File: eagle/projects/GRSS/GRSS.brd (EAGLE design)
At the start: 66 x 62.1 mm, 37 parts, among them J1 MOL-SL-2-RA, J10 MOL-SL-2-RA, J11 MOL-SL-2-V, J2 MOL-SL-2-RA, J3 MOL-SL-2-RA, J4 MOL-SL-2-RA, J5 MOL-SL-2-RA, J6 MOL-SL-2-RA, J7 MOL-SL-2-RA, J8 MOL-SL-2-RA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

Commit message: Squad Logo / 2-layer
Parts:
- removed IMAGE1: SQUAD_LOGO, grss:SQUAD_LOGO
- added LOGO1: (no value), grss:SQUAD_LOGO
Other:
- board text added: "Lincoln Glauser P17105: HABIP SPRING 2017 XXX-XXX-XX"
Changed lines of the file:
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@@
 <text x="16.2" y="28.1" size="1.016" layer="25" ratio="15">LDO</text>
 <text x="34.1" y="28.5" size="1.016" layer="25" ratio="15">555</text>
+<text x="48.5" y="32.6" size="1.016" layer="21" ratio="15">Lincoln Glauser
+P17105: HABIP
+SPRING 2017
+XXX-XXX-XX</text>
 </plain>
 <attributes>
@@
 <attribute name="VALUE" x="49.56" y="23.5" size="0.254" layer="27" ratio="6" align="center"/>
 </element>
-<element name="IMAGE1" library="grss" package="SQUAD_LOGO" value="SQUAD_LOGO" x="41.6" y="33.3"/>
+<element name="LOGO1" library="grss" package="SQUAD_LOGO" value="" x="41.2" y="34.1">
+<attribute name="_EXTERNAL_" value="" x="41.2" y="34.1" size="1.778" layer="27" display="off"/>
+</element>
 </elements>
 <signals>
@@
 </board>
 </drawing>
+<compatibility>
+<note version="6.3" minversion="6.2.2" severity="warning">
+Since Version 6.2.2 text objects can contain more than one line,
+which will not be processed correctly with this version.
+</note>
+</compatibility>
 </eagle>

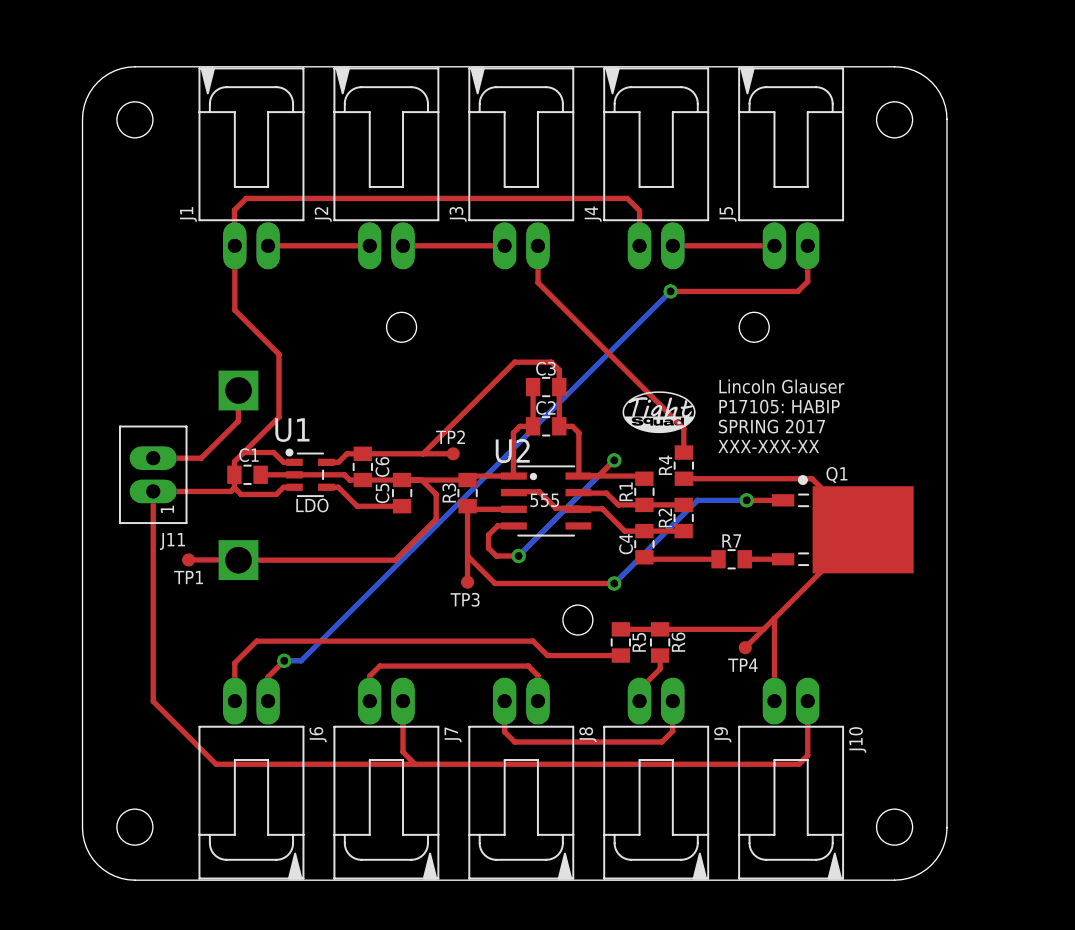
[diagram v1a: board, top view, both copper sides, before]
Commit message: GND / Power Planes - LG
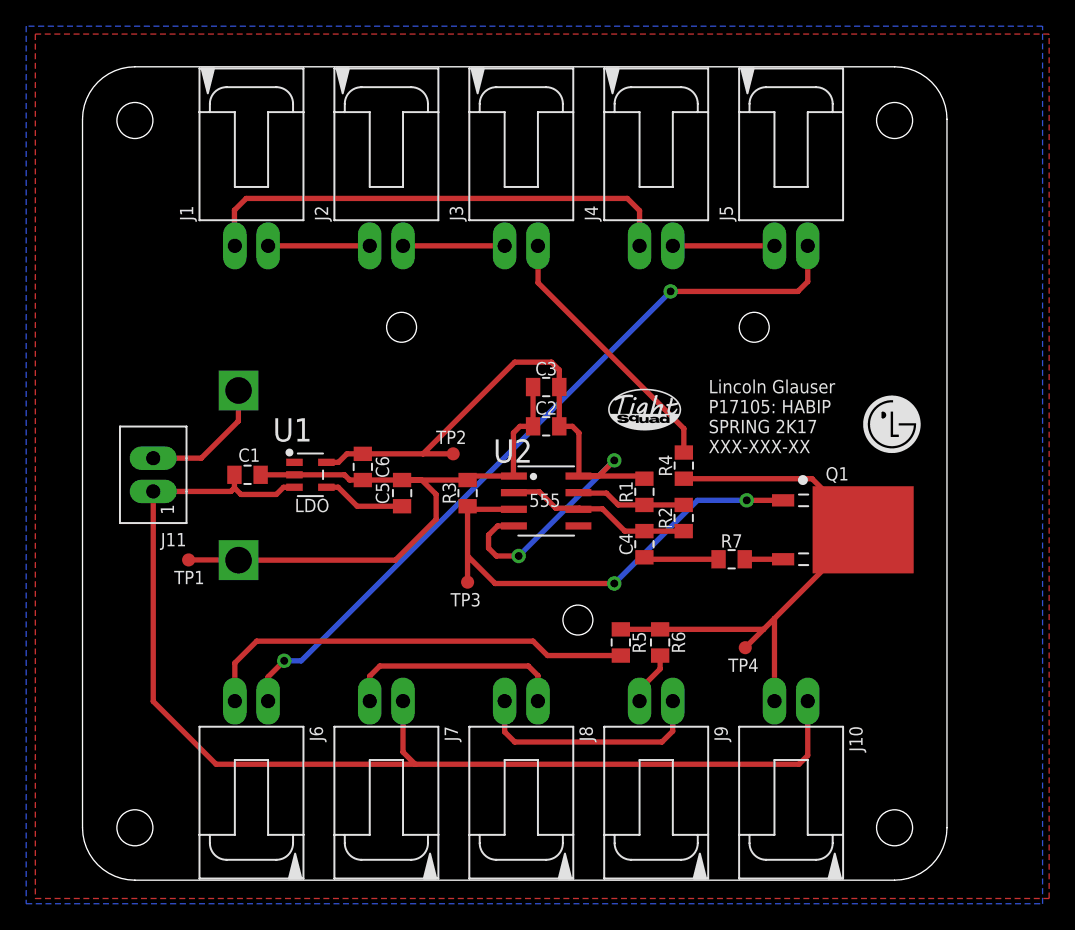
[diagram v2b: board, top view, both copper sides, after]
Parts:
- added E$1: (no value), grss:LG
- moved LOGO1 1.12 mm to (40.1, 34.3)
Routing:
- net 9V0: track 151.5 -> 127.1 mm
- added copper zone on layer 1, net 9V0
- added copper zone on layer 16, net GND
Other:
- board text added: "Lincoln Glauser P17105: HABIP SPRING 2K17 XXX-XXX-XX"
- board text removed: "Lincoln Glauser P17105: HABIP SPRING 2017 XXX-XXX-XX"
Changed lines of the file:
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@@
 <layers>
 <layer number="1" name="Top" color="4" fill="1" visible="yes" active="yes"/>
-<layer number="2" name="Route2" color="1" fill="3" visible="yes" active="yes"/>
+<layer number="2" name="Route2" color="1" fill="3" visible="no" active="no"/>
 <layer number="3" name="Route3" color="4" fill="3" visible="no" active="no"/>
 <layer number="14" name="Route14" color="1" fill="6" visible="no" active="no"/>
-<layer number="15" name="Route15" color="4" fill="6" visible="yes" active="yes"/>
+<layer number="15" name="Route15" color="4" fill="6" visible="no" active="no"/>
 <layer number="16" name="Bottom" color="1" fill="1" visible="yes" active="yes"/>
 <layer number="17" name="Pads" color="2" fill="1" visible="yes" active="yes"/>
@@
 <text x="16.2" y="28.1" size="1.016" layer="25" ratio="15">LDO</text>
 <text x="34.1" y="28.5" size="1.016" layer="25" ratio="15">555</text>
-<text x="48.5" y="32.6" size="1.016" layer="21" ratio="15">Lincoln Glauser
+<text x="47.8" y="32.6" size="1.016" layer="21" ratio="15">Lincoln Glauser
 P17105: HABIP
-SPRING 2017
+SPRING 2K17
 XXX-XXX-XX</text>
 </plain>
@@
 </class>
 </classes>
-<designrules name="4layer_4pcb">
+<designrules name="2layer_2pcb">
 <description language="de">&lt;b&gt;EAGLE Design Rules&lt;/b&gt;
 &lt;p&gt;
@@
 <description language="en">&lt;b&gt;EAGLE Design Rules&lt;/b&gt;
 &lt;p&gt;
-Modified for $66 4-layer student special from Advanced Circuits as of 02/07/2017. These specs also meet the standard specs at PCBWay as of 02/07/2017</description>
-<param name="layerSetup" value="(1+2*15+16)"/>
+Modified for $66 4-layer student special from Advanced Circuits as of 02/07/2017. These specs also meet the standard specs at PCBWay as of 02/07/2017. Updated layerSetup for 2-layer.</description>
+<param name="layerSetup" value="(1+16)"/>
 <param name="mtCopper" value="0.035mm 0.035mm 0.035559375mm 0.035559375mm 0.035559375mm 0.035559375mm 0.035559375mm 0.035559375mm 0.035559375mm 0.035559375mm 0.035559375mm 0.035559375mm 0.035559375mm 0.035559375mm 0.035mm 0.035mm"/>
 <param name="mtIsolate" value="0.486mm 0.488mm 0.200659375mm 0.149859375mm 0.200659375mm 0.149859375mm 0.200659375mm 0.149859375mm 0.200659375mm 0.149859375mm 0.200659375mm 0.149859375mm 0.200659375mm 0.149859375mm 0.486mm"/>
@@
 <attribute name="VALUE" x="51.119" y="16.942" size="0.254" layer="27" ratio="6"/>
 </element>
-<element name="H1" library="grss" package="2,75_HOLE_RASPI" value="MOUNT-HOLE_2.75" x="4" y="4.05"/>
-<element name="H2" library="grss" package="2,75_HOLE_RASPI" value="MOUNT-HOLE_2.75" x="62" y="4.05"/>
-<element name="H3" library="grss" package="2,75_HOLE_RASPI" value="MOUNT-HOLE_2.75" x="4" y="58.05"/>
-<element name="H4" library="grss" package="2,75_HOLE_RASPI" value="MOUNT-HOLE_2.75" x="62" y="58.05"/>
+<element name="H1" library="grss" package="2,75_HOLE_RASPI" value="MOUNT-HOLE_2.75" x="4" y="4"/>
+<element name="H2" library="grss" package="2,75_HOLE_RASPI" value="MOUNT-HOLE_2.75" x="62" y="4"/>
+<element name="H3" library="grss" package="2,75_HOLE_RASPI" value="MOUNT-HOLE_2.75" x="4" y="58"/>
+<element name="H4" library="grss" package="2,75_HOLE_RASPI" value="MOUNT-HOLE_2.75" x="62" y="58"/>
 <element name="R3" library="grss" package="R0805" value="4.7k" x="29.4" y="29.55" smashed="yes" rot="R270">
 <attribute name="TOLERANCE" value="1%" x="29.4" y="29.55" size="1.778" layer="27" rot="R270" display="off"/>
@@
 <attribute name="VALUE" x="49.56" y="23.5" size="0.254" layer="27" ratio="6" align="center"/>
 </element>
-<element name="LOGO1" library="grss" package="SQUAD_LOGO" value="" x="41.2" y="34.1">
-<attribute name="_EXTERNAL_" value="" x="41.2" y="34.1" size="1.778" layer="27" display="off"/>
-</element>
+<element name="LOGO1" library="grss" package="SQUAD_LOGO" value="" x="40.1" y="34.3">
+<attribute name="_EXTERNAL_" value="" x="40.1" y="34.3" size="1.778" layer="27" display="off"/>
+</element>
+<element name="E$1" library="grss" package="LG" value="" x="59.6" y="32.6"/>
 </elements>
 <signals>
@@
 <contactref element="J10" pad="1"/>
 <contactref element="J11" pad="1"/>
-<wire x1="16.1808" y1="31.9025" x2="16.1293" y2="31.901" width="0.4064" layer="1"/>
-<wire x1="16.1293" y1="31.901" x2="15.349" y2="31.901" width="0.4064" layer="1"/>
-<wire x1="15.349" y1="31.901" x2="14.6" y2="32.65" width="0.4064" layer="1"/>
-<wire x1="14.6" y1="32.65" x2="12.3" y2="32.65" width="0.4064" layer="1"/>
-<wire x1="12.3" y1="32.65" x2="11.6" y2="31.95" width="0.4064" layer="1"/>
-<wire x1="11.6" y1="31.95" x2="11.6" y2="30.95" width="0.4064" layer="1"/>
 <wire x1="11.6" y1="29.95" x2="11.6" y2="30.95" width="0.4064" layer="1"/>
 <wire x1="16.1808" y1="29.9975" x2="15.3475" y2="29.9975" width="0.4064" layer="1"/>
@@
 <wire x1="11.6" y1="51.15" x2="11.6" y2="48.46" width="0.4064" layer="1"/>
 <wire x1="11.6" y1="48.46" x2="11.63" y2="48.43" width="0.4064" layer="1"/>
-<wire x1="11.63" y1="48.43" x2="11.63" y2="43.52" width="0.4064" layer="1"/>
-<wire x1="11.63" y1="43.52" x2="15" y2="40.15" width="0.4064" layer="1"/>
-<wire x1="15" y1="40.15" x2="15" y2="35.35" width="0.4064" layer="1"/>
-<wire x1="15" y1="35.35" x2="12.3" y2="32.65" width="0.4064" layer="1"/>
 <wire x1="5.4" y1="29.68" x2="11.33" y2="29.68" width="0.4064" layer="1"/>
 <wire x1="11.33" y1="29.68" x2="11.6" y2="29.95" width="0.4064" layer="1"/>
@@
 <wire x1="5.4" y1="13.65" x2="5.4" y2="29.68" width="0.4064" layer="1"/>
 <wire x1="24.47" y1="9.78" x2="25.4" y2="8.85" width="0.4064" layer="1"/>
+<polygon width="0.4064" layer="1">
+<vertex x="-3.6" y="64.6"/>
+<vertex x="-3.6" y="-1.4"/>
+<vertex x="73.8" y="-1.4"/>
+<vertex x="73.8" y="64.6"/>
+</polygon>
 </signal>
 <signal name="GND">
@@
 <wire x1="25.9" y1="30.55" x2="24.4" y2="30.55" width="0.4064" layer="1"/>
 <wire x1="29.4" y1="30.55" x2="24.4" y2="30.55" width="0.4064" layer="1"/>
-<wire x1="32.9362" y1="30.855" x2="42.9" y2="24.65" width="0" layer="19" extent="1-1"/>
 <wire x1="8.1" y1="24.45" x2="11.896" y2="24.45" width="0.4064" layer="1"/>
 <wire x1="11.896" y1="24.45" x2="11.914" y2="24.432" width="0.4064" layer="1"/>
+<polygon width="0.4064" layer="16">
+<vertex x="-4.3" y="65.2"/>
+<vertex x="-4.3" y="-1.8"/>
+<vertex x="73.3" y="-1.8"/>
+<vertex x="73.3" y="65.2"/>
+</polygon>
+<wire x1="32.9362" y1="30.855" x2="42.9" y2="24.65" width="0" layer="19" extent="1-1"/>
 </signal>
 <signal name="THRTRIG">

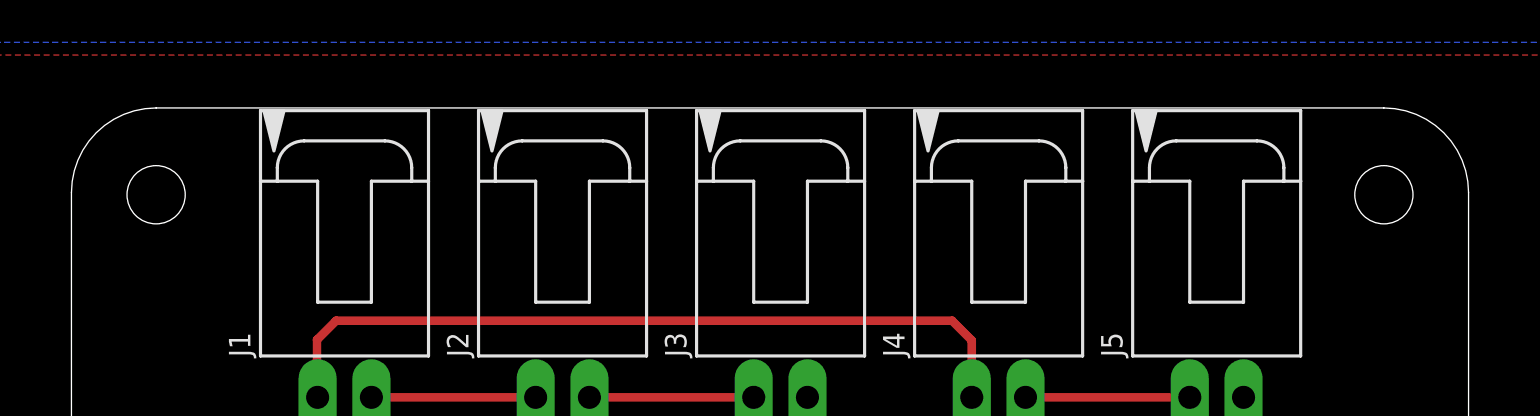
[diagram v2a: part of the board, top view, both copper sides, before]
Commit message: moved mounting holes briefly
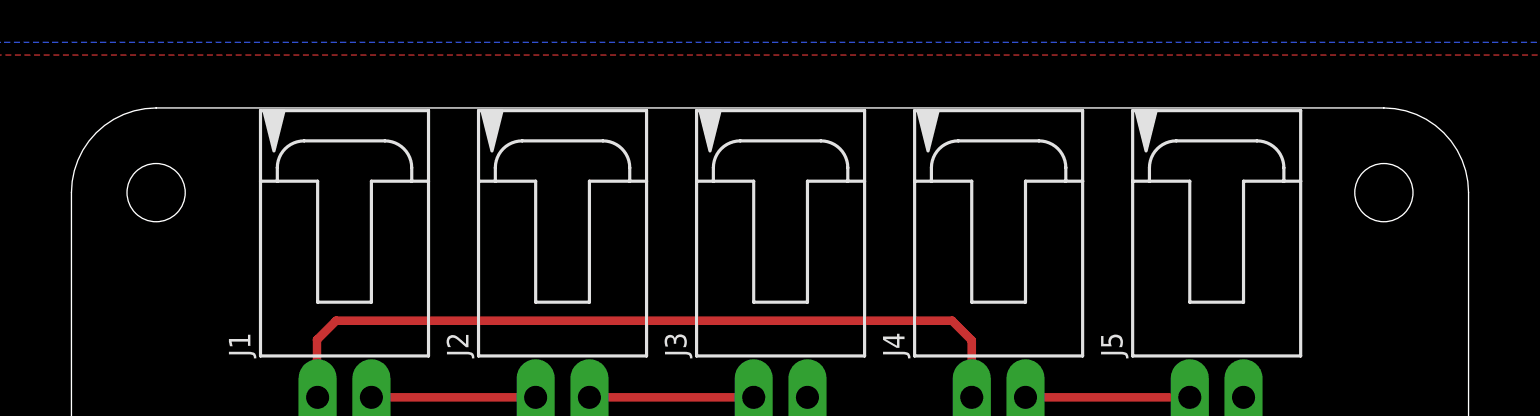
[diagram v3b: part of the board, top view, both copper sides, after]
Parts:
- LOGO1: value (none) -> LOGO
- moved H3 0.10 mm to (4.00, 58.1)
- moved H4 0.10 mm to (62.0, 58.1)
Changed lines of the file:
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@@
 <element name="H1" library="grss" package="2,75_HOLE_RASPI" value="MOUNT-HOLE_2.75" x="4" y="4"/>
 <element name="H2" library="grss" package="2,75_HOLE_RASPI" value="MOUNT-HOLE_2.75" x="62" y="4"/>
-<element name="H3" library="grss" package="2,75_HOLE_RASPI" value="MOUNT-HOLE_2.75" x="4" y="58"/>
-<element name="H4" library="grss" package="2,75_HOLE_RASPI" value="MOUNT-HOLE_2.75" x="62" y="58"/>
+<element name="H3" library="grss" package="2,75_HOLE_RASPI" value="MOUNT-HOLE_2.75" x="4" y="58.1"/>
+<element name="H4" library="grss" package="2,75_HOLE_RASPI" value="MOUNT-HOLE_2.75" x="62" y="58.1"/>
 <element name="R3" library="grss" package="R0805" value="4.7k" x="29.4" y="29.55" smashed="yes" rot="R270">
 <attribute name="TOLERANCE" value="1%" x="29.4" y="29.55" size="1.778" layer="27" rot="R270" display="off"/>
@@
 <attribute name="VALUE" x="49.56" y="23.5" size="0.254" layer="27" ratio="6" align="center"/>
 </element>
-<element name="LOGO1" library="grss" package="SQUAD_LOGO" value="" x="40.1" y="34.3">
+<element name="LOGO1" library="grss" package="SQUAD_LOGO" value="LOGO" x="40.1" y="34.3">
 <attribute name="_EXTERNAL_" value="" x="40.1" y="34.3" size="1.778" layer="27" display="off"/>
 </element>

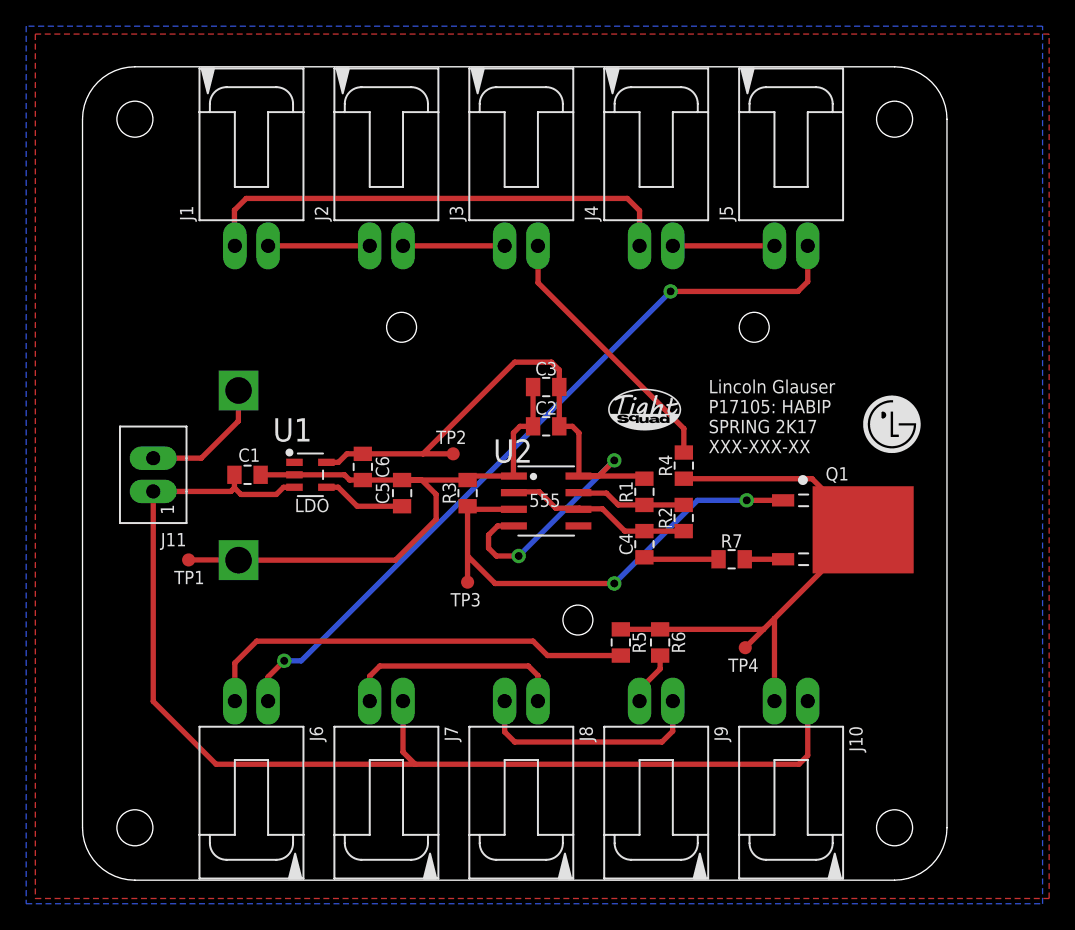
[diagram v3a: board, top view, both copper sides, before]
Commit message: Mark updates... 25 mil on some traces that have 10-15mA current and heat sink section for Power FET
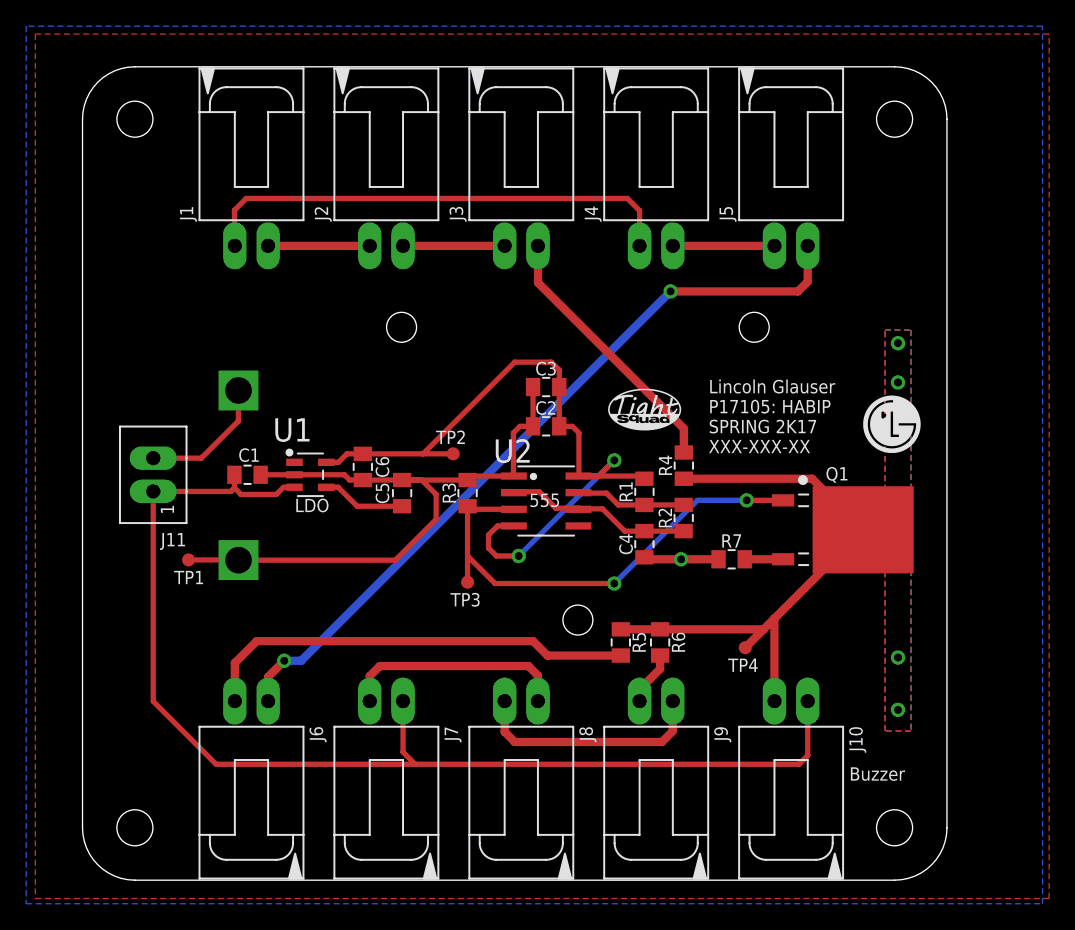
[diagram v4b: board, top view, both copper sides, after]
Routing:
- net VD: vias 0 -> 4
- net GND: vias 0 -> 1
- added copper zone on layer 1, net VD
- added copper zone on layer 16, net VD
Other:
- board text added: "Buzzer"
